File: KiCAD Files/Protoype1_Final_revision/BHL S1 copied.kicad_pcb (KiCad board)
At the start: 4 copper layers, 64 x 64 mm, 106 parts, among them IC1 NUP2105LT1G, IC2 NUP2105LT1G, IC3 IR2136STRPBF, J1 39-30-1042, J2 Conn_01x03_Pin, J3 Conn_01x03_Pin, J4 39-30-1042, Q1 CSD19502Q5B, Q2 CSD19502Q5B, Q3 CSD19502Q5B, Q4 CSD19502Q5B, Q5 CSD19502Q5B, Q7 CSD19502Q5B, U1 ME6211C30M5, U2 SPX3819M5-L-5-0, U3 Solder Pad, U5 STM32G431CBU6, Y1 8MHz, Y2 8MHz

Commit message: Resonator footprint updated
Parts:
- Y1: footprint Footprint for BHL S1:CSTNE8M00G520000R0_Resonator -> Footprint for BHL S1:CSTNE8M00G55Z000R0_Resonator
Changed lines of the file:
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@@
 		)
 	)
-	(footprint "Footprint for BHL S1:CSTNE8M00G520000R0_Resonator"
+	(footprint "Footprint for BHL S1:CSTNE8M00G55Z000R0_Resonator"
 		(layer "F.Cu")
 		(at 148.8925 96.335)
-		(descr "CSTNE8M00G520000R0-2")
+		(descr "CSTNE8M00G55Z000R0-2")
 		(tags "Crystal or Oscillator")
 		(property "Reference" "Y1"
@@
 		(attr smd)
 		(fp_line
-			(start 2.1 0)
-			(end 2.1 0)
-			(stroke
-				(width 0.1)
-				(type solid)
-			)
-			(layer "F.SilkS")
-		)
-		(fp_line
-			(start 2.2 0)
-			(end 2.2 0)
-			(stroke
-				(width 0.1)
-				(type solid)
-			)
-			(layer "F.SilkS")
-		)
-		(fp_arc
-			(start 2.1 0)
-			(mid 2.15 -0.05)
-			(end 2.2 0)
-			(stroke
-				(width 0.1)
-				(type solid)
-			)
-			(layer "F.SilkS")
-		)
-		(fp_arc
-			(start 2.2 0)
-			(mid 2.15 0.05)
-			(end 2.1 0)
-			(stroke
-				(width 0.1)
-				(type solid)
-			)
-			(layer "F.SilkS")
-		)
-		(fp_line
-			(start -2.6 -1.95)
-			(end 2.6 -1.95)
-			(stroke
-				(width 0.1)
-				(type solid)
-			)
-			(layer "F.CrtYd")
-		)
-		(fp_line
-			(start -2.6 1.95)
-			(end -2.6 -1.95)
-			(stroke
-				(width 0.1)
-				(type solid)
-			)
-			(layer "F.CrtYd")
-		)
-		(fp_line
-			(start 2.6 -1.95)
-			(end 2.6 1.95)
-			(stroke
-				(width 0.1)
-				(type solid)
-			)
-			(layer "F.CrtYd")
-		)
-		(fp_line
-			(start 2.6 1.95)
-			(end -2.6 1.95)
-			(stroke
-				(width 0.1)
-				(type solid)
-			)
-			(layer "F.CrtYd")
-		)
-		(fp_line
 			(start -1.6 -0.65)
-			(end 1.6 -0.65)
-			(stroke
-				(width 0.1)
-				(type solid)
-			)
-			(layer "F.Fab")
-		)
-		(fp_line
-			(start -1.6 0.65)
-			(end -1.6 -0.65)
-			(stroke
-				(width 0.1)
-				(type solid)
-			)
-			(layer "F.Fab")
+			(end -1.6 0.65)
+			(stroke
+				(width 0.1)
+				(type solid)
+			)
+			(layer "F.SilkS")
+		)
+		(fp_line
+			(start 1.1 1.3)
+			(end 1.1 1.3)
+			(stroke
+				(width 0.2)
+				(type solid)
+			)
+			(layer "F.SilkS")
+		)
+		(fp_line
+			(start 1.3 1.3)
+			(end 1.3 1.3)
+			(stroke
+				(width 0.2)
+				(type solid)
+			)
+			(layer "F.SilkS")
 		)
 		(fp_line
@@
 				(type solid)
 			)
+			(layer "F.SilkS")
+		)
+		(fp_arc
+			(start 1.1 1.3)
+			(mid 1.2 1.2)
+			(end 1.3 1.3)
+			(stroke
+				(width 0.2)
+				(type solid)
+			)
+			(layer "F.SilkS")
+		)
+		(fp_arc
+			(start 1.3 1.3)
+			(mid 1.2 1.4)
+			(end 1.1 1.3)
+			(stroke
+				(width 0.2)
+				(type solid)
+			)
+			(layer "F.SilkS")
+		)
+		(fp_line
+			(start -2.6 -1.95)
+			(end -2.6 1.95)
+			(stroke
+				(width 0.1)
+				(type solid)
+			)
+			(layer "F.CrtYd")
+		)
+		(fp_line
+			(start -2.6 1.95)
+			(end 2.6 1.95)
+			(stroke
+				(width 0.1)
+				(type solid)
+			)
+			(layer "F.CrtYd")
+		)
+		(fp_line
+			(start 2.6 -1.95)
+			(end -2.6 -1.95)
+			(stroke
+				(width 0.1)
+				(type solid)
+			)
+			(layer "F.CrtYd")
+		)
+		(fp_line
+			(start 2.6 1.95)
+			(end 2.6 -1.95)
+			(stroke
+				(width 0.1)
+				(type solid)
+			)
+			(layer "F.CrtYd")
+		)
+		(fp_line
+			(start -1.6 -0.65)
+			(end -1.6 0.65)
+			(stroke
+				(width 0.2)
+				(type solid)
+			)
+			(layer "F.Fab")
+		)
+		(fp_line
+			(start -1.6 0.65)
+			(end 1.6 0.65)
+			(stroke
+				(width 0.2)
+				(type solid)
+			)
+			(layer "F.Fab")
+		)
+		(fp_line
+			(start 1.6 -0.65)
+			(end -1.6 -0.65)
+			(stroke
+				(width 0.2)
+				(type solid)
+			)
 			(layer "F.Fab")
 		)
 		(fp_line
 			(start 1.6 0.65)
-			(end -1.6 0.65)
-			(stroke
-				(width 0.1)
+			(end 1.6 -0.65)
+			(stroke
+				(width 0.2)
 				(type solid)
 			)
@@
 		)
 		(embedded_fonts no)
+		(model "C:/Users/jiaxi/Downloads/LIB_CSTNE8M00G55Z000R0/CSTNE8M00G55Z000R0/3D/CSTNE8M00G55Z000R0.stp"
+			(offset
+				(xyz 0 0 0)
+			)
+			(scale
+				(xyz 1 1 1)
+			)
+			(rotate
+				(xyz -90 -0 -0)
+			)
+		)
 	)
 	(footprint "Capacitor_SMD:C_0402_1005Metric_Pad0.74x0.62mm_HandSolder"

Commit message: Worked on the PCB layout
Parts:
- removed Y2: 8MHz, Footprint for BHL S1:AWSCR800CELAC10T3_Resonator
- moved J2 101.2 mm to (168.6, 93.5), turned to -90 degrees
- moved L1 64.1 mm to (214.5, 90.8)
- moved IC1 61.3 mm to (205.8, 89.6)
- moved IC2 61.3 mm to (205.8, 94.2)
- moved VR1 58.7 mm to (172.2, 67.5)
- moved U1 48.7 mm to (190.4, 93.5)
- moved U2 46.1 mm to (195.1, 93.5), turned to 180 degrees
- moved IC3 44.7 mm to (156.8, 57.4), turned to -45 degrees
- moved U5 42.3 mm to (192.8, 85.8)
- moved Q1 40.1 mm to (195.8, 63.2), turned to -135 degrees
- moved U3 38.9 mm to (213.0, 65.5), turned to -45 degrees
- moved Y1 38.7 mm to (186.2, 86.2), turned to 90 degrees
- moved Q2 35.7 mm to (199.5, 67.1), turned to -135 degrees
- moved Q3 31.2 mm to (203.4, 70.9), turned to -135 degrees
- moved TCAN1051HGVDR1 28.0 mm to (177.7, 94.4)
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
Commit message: update PCB
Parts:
- moved R9 31.8 mm to (191.6, 66.4), turned to 45 degrees
- moved IC3 5.95 mm to (151.0, 58.8)
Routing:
- net Vshunt_1+: track 0.00 -> 4.43 mm
- added copper zone on In1.Cu, net GND
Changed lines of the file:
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@@
 	(paper "A4")
 	(layers
-		(0 "F.Cu" signal)
-		(4 "In1.Cu" signal)
-		(6 "In2.Cu" signal)
-		(2 "B.Cu" signal)
+		(0 "F.Cu" mixed "Signal.Power1")
+		(4 "In1.Cu" power "GND")
+		(6 "In2.Cu" power "Power")
+		(2 "B.Cu" mixed "Signal.Power2")
 		(9 "F.Adhes" user "F.Adhesive")
 		(11 "B.Adhes" user "B.Adhesive")
@@
 		(fp_arc
 			(start -6.975 0)
-			(mid -6.95 -0.025001)
+			(mid -6.950001 -0.025001)
 			(end -6.925 0.000001)
 			(stroke
@@
 	(footprint "Resistor_SMD:R_0402_1005Metric_Pad0.72x0.64mm_HandSolder"
 		(layer "F.Cu")
-		(at 211.3825 41.49)
+		(at 191.577504 66.422496 45)
 		(descr "Resistor SMD 0402 (1005 Metric), square (rectangular) end terminal, IPC-7351 nominal with elongated pad for handsoldering. (Body size source: IPC-SM-782 page 72, https://www.pcb-3d.com/wordpress/wp-content/uploads/ipc-sm-782a_amendment_1_and_2.pdf), generated with kicad-footprint-generator")
 		(tags "resistor handsolder")
 		(property "Reference" "R9"
-			(at 0 -1.17 0)
+			(at 0 -1.17 45)
 			(layer "F.SilkS")
 			(effects
@@
 		)
 		(property "Value" "1.5K"
-			(at 0 1.17 0)
+			(at 0 1.17 45)
 			(layer "F.Fab")
 			(effects
@@
 		)
 		(property "Datasheet" "~"
-			(at 0 0 0)
+			(at 0 0 45)
 			(layer "F.Fab")
 			(hide yes)
@@
 		)
 		(property "Description" "Resistor"
-			(at 0 0 0)
+			(at 0 0 45)
 			(layer "F.Fab")
 			(hide yes)
@@
 		(attr smd)
 		(fp_line
-			(start -0.167621 -0.38)
-			(end 0.167621 -0.38)
+			(start -0.167621 -0.380001)
+			(end 0.167621 -0.380001)
 			(stroke
 				(width 0.12)
@@
 		)
 		(fp_line
-			(start -0.167621 0.38)
-			(end 0.167621 0.38)
+			(start -0.167621 0.380001)
+			(end 0.167621 0.380001)
 			(stroke
 				(width 0.12)
@@
 		)
 		(fp_text user "${REFERENCE}"
-			(at 0 0 0)
+			(at 0 0 45)
 			(layer "F.Fab")
 			(effects
@@
 		)
 		(pad "1" smd roundrect
-			(at -0.5975 0)
+			(at -0.5975 0 45)
 			(size 0.715 0.64)
 			(layers "F.Cu" "F.Mask" "F.Paste")
@@
 		)
 		(pad "2" smd roundrect
-			(at 0.5975 0)
+			(at 0.5975 0 45)
 			(size 0.715 0.64)
 			(layers "F.Cu" "F.Mask" "F.Paste")
@@
 	(footprint "Footprint for BHL S1:3PHASE_GATE_DRIVER"
 		(layer "F.Cu")
-		(at 156.790772 57.373002 -45)
+		(at 151 58.75 -45)
 		(descr "28-LEAD SOIC")
 		(tags "Integrated Circuit")
@@
 		)
 		(embedded_fonts no)
-		(model "C:/Users/jiaxi/Downloads/LIB_CSTNE8M00G55Z000R0/CSTNE8M00G55Z000R0/3D/CSTNE8M00G55Z000R0.stp"
+		(model "/Users/elijahrobinson/Documents/GitHub/Robot-Dog/KiCAD Files/3D models/CSTNE8M00G55Z000R0_Resonator.stp"
 			(offset
 				(xyz 0 0 0)
@@
 		(layer "Edge.Cuts")
 	)
+	(segment
+		(start 192 66)
+		(end 192.058381 66)
+		(width 0.2)
+		(layer "F.Cu")
+		(net 37)
+	)
+	(segment
+		(start 193.351974 64.706407)
+		(end 194.25 65.604433)
+		(width 0.2)
+		(layer "F.Cu")
+		(net 37)
+	)
+	(segment
+		(start 192.453949 63.808381)
+		(end 193.351974 64.706407)
+		(width 0.2)
+		(layer "F.Cu")
+		(net 37)
+	)
+	(segment
+		(start 192.058381 66)
+		(end 193.351974 64.706407)
+		(width 0.2)
+		(layer "F.Cu")
+		(net 37)
+	)
+	(zone
+		(net 5)
+		(net_name "GND")
+		(layer "In1.Cu")
+		(hatch edge 0.5)
+		(connect_pads
+			(clearance 0.5)
+		)
+		(min_thickness 0.25)
+		(filled_areas_thickness no)
+		(fill
+			(thermal_gap 0.5)
+			(thermal_bridge_width 0.5)
+		)
+		(polygon
+			(pts
+				(xy 160.135093 53.540419) (xy 224.635093 53.790419) (xy 224.385093 118.040419) (xy 160.385093 117.790419)
+			)
+		)
+	)
 	(group ""

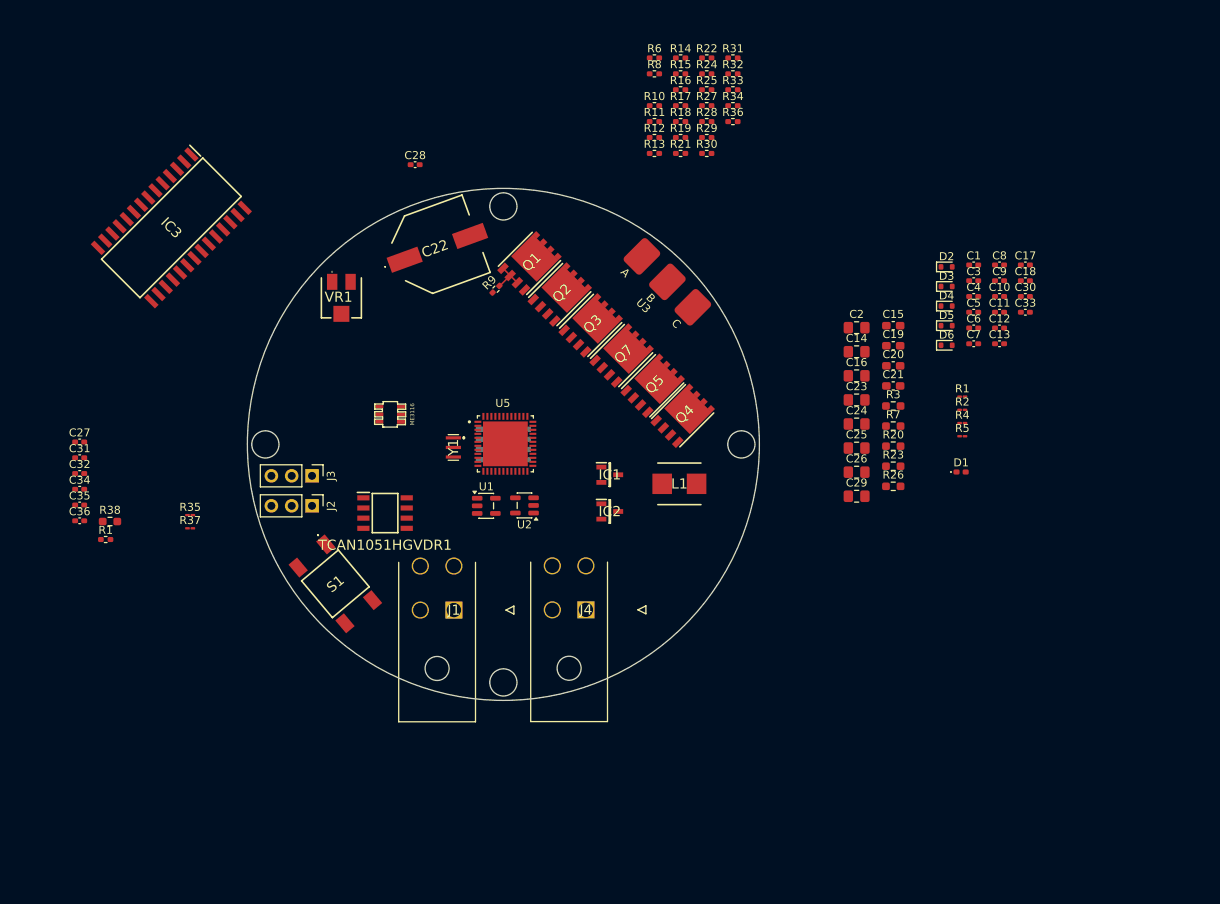
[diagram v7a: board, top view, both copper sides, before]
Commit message: Footprint and 3d model updated, PCB updated
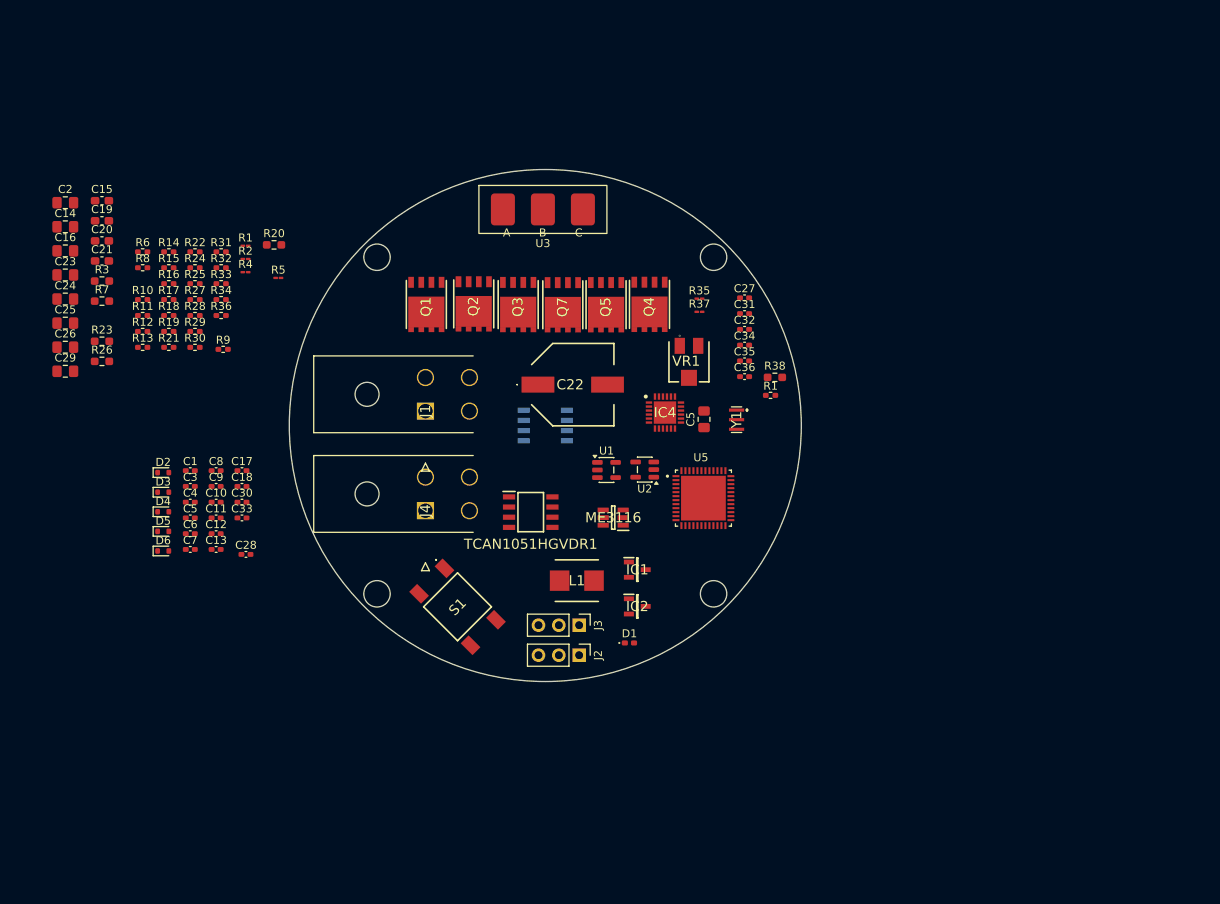
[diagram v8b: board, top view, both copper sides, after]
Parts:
- removed IC3: IR2136STRPBF, Footprint for BHL S1:3PHASE_GATE_DRIVER
- added C5: 10uF/35V, Capacitor_SMD:C_0805_2012Metric_Pad1.18x1.45mm_HandSolder, F.Cu at (217.6, 82.7)
- added IC4: FD6288Q, Footprint for BHL S1:QFN50P400X400X90-25N-D_Gatedriver1, F.Cu at (212.7, 81.8)
- ME3116: footprint Footprint for BHL S1:ME3116AM6G_Regulator -> Footprint for BHL S1:SOT95P270X145-6N_ME3116
- U5: footprint Footprint for BHL S1:QFN50P700X700X60-49N -> Footprint for BHL S1:QFN50P700X700X60-49N_STM32
- moved C10 101.2 mm to (156.6, 93.0)
- moved C11 101.2 mm to (156.6, 95.0)
- moved C12 101.2 mm to (156.6, 97.0)
- moved C13 101.2 mm to (156.6, 99.0)
- moved C8 101.2 mm to (156.6, 89.1)
- moved C9 101.2 mm to (156.6, 91.1)
- moved C1 101.2 mm to (153.4, 89.1)
- moved C17 101.2 mm to (159.8, 89.1)
- moved C18 101.2 mm to (159.8, 91.1)
- moved C3 101.2 mm to (153.4, 91.1)
- moved C30 101.2 mm to (159.8, 93.0)
- moved C33 101.2 mm to (159.8, 95.0)
- moved C4 101.2 mm to (153.4, 93.0)
- moved C5 101.2 mm to (153.4, 95.0)
- moved C6 101.2 mm to (153.4, 97.0)
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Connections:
- J3 pad 1: Net-(J3-Pin_1) -> GND
- J3 pad 2: GND -> Net-(J3-Pin_2)
- U5 pad 42: Net-(J3-Pin_1) -> Net-(J3-Pin_2)
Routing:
- net Vshunt_1+: track 4.43 -> 0.00 mm
- removed copper zone on In1.Cu, net GND
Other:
- outline, holes or cut-outs redrawn
